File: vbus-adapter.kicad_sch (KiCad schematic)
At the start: 54 parts, among them J1 VBUS, J2 CAN, J3 Sens 2, J4 Sens 1, J5 Power, J6 Backup GPIO, J7 Program, Q1 SS8050, Q2 SS8050, T800 AO3400A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

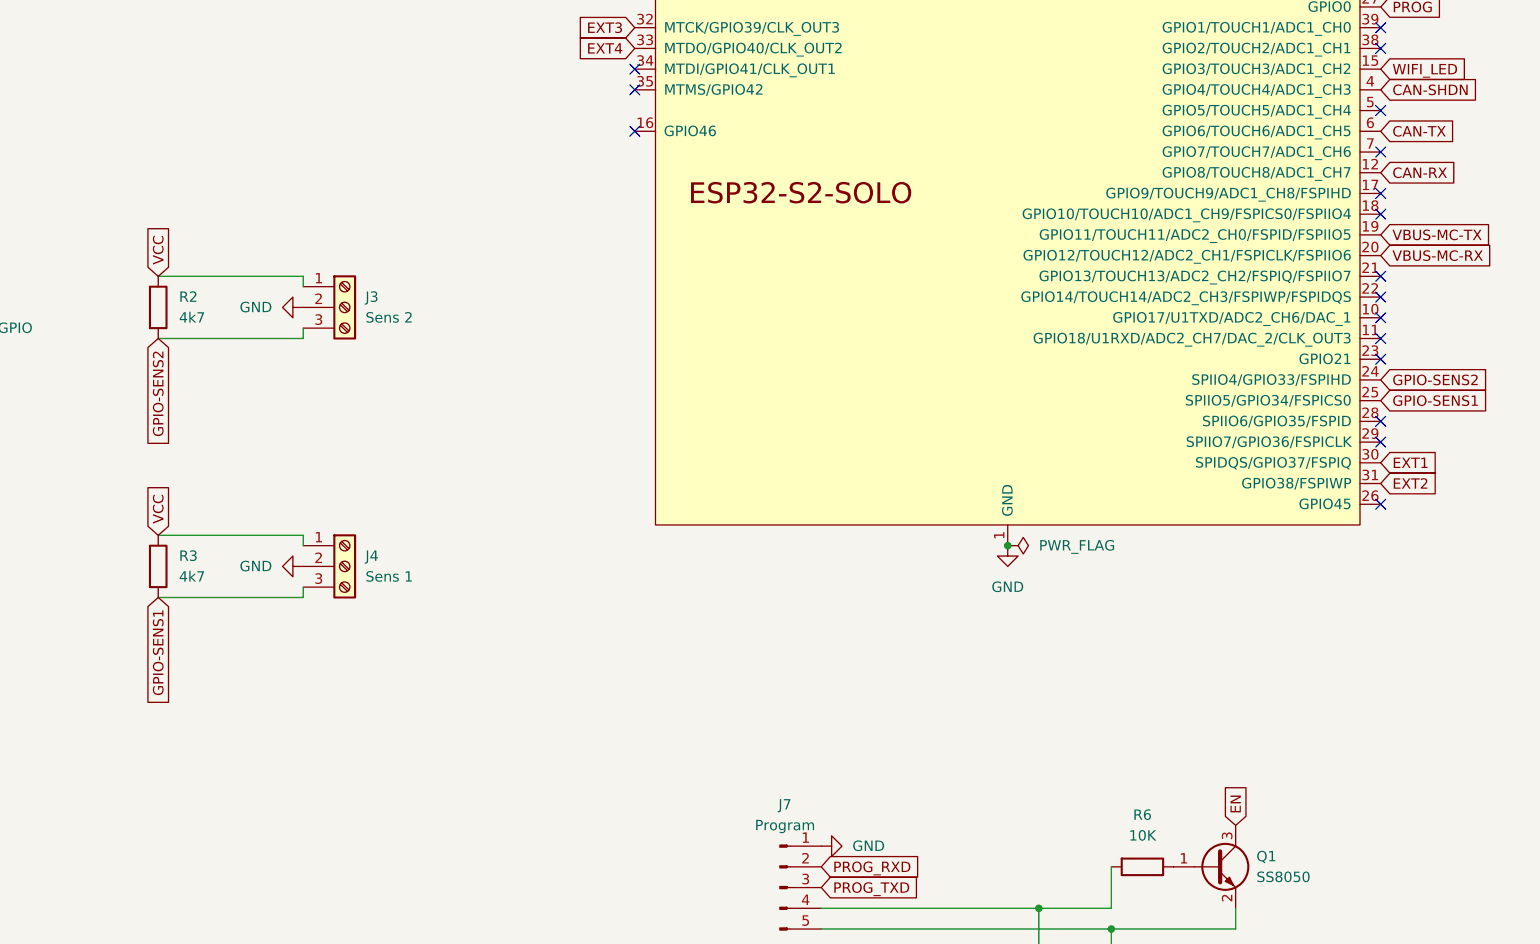
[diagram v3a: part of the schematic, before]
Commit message: Version 5
- Reposition connectors for Programming
- Add +5V to Sensor Connector
- Make VCC on SENS connector from GPIO
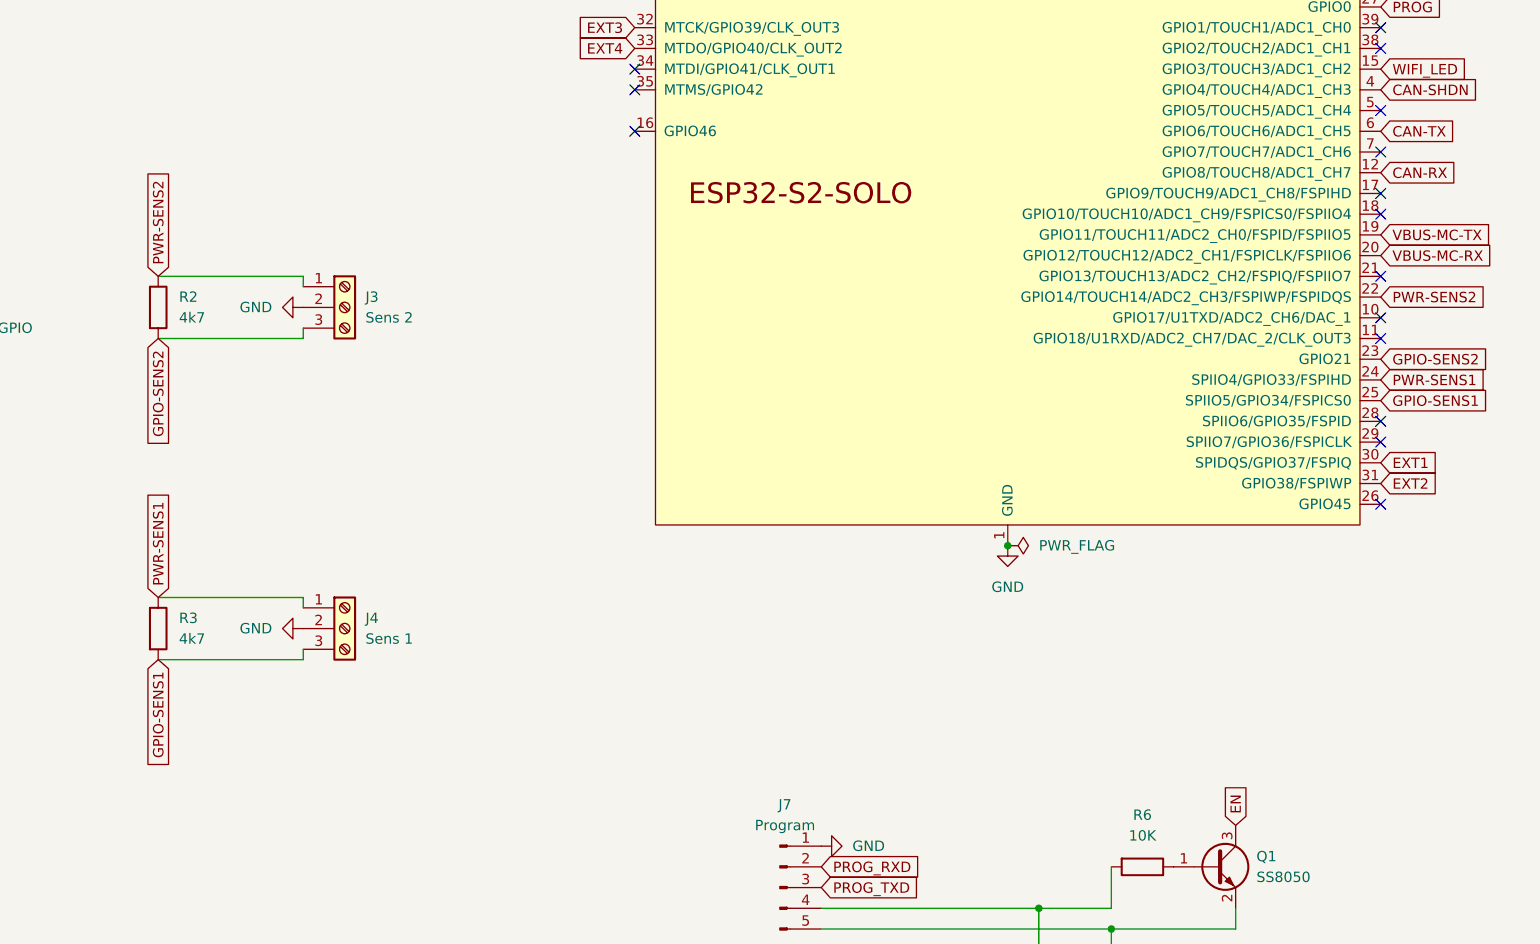
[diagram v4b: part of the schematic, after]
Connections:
- net GPIO-SENS2: now also U2.23 (GPIO21); no longer U2.24 (SPIIO4/GPIO33/FSPIHD)
- net VCC: no longer J3.1 (Pin_1), J4.1 (Pin_1), R2.1, R3.1
- net PWR-SENS2: now reaches U2.22 (GPIO14/TOUCH14/ADC2_CH3/FSPIWP/FSPIDQS)
- net PWR-SENS2: now also J3.1 (Pin_1), R2.1
- new net PWR-SENS1: J4.1 (Pin_1), R3.1, U2.24 (SPIIO4/GPIO33/FSPIHD)
- no-connect marks 22 -> 20
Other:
- moved on the sheet: J4, R3
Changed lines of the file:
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@@
 		(title "vbus-adapter")
 		(date "2026-04-29")
-		(rev "v4")
+		(rev "v5")
 	)
 	(junction
@@
 	)
 	(no_connect
-		(at 370.84 111.76)
-	)
-	(no_connect
 		(at 370.84 91.44)
 	)
@@
 	)
 	(no_connect
-		(at 370.84 104.14)
-	)
-	(no_connect
 		(at 370.84 81.28)
 	)
@@
 	(wire
 		(pts
-			(xy 238.76 140.97) (xy 238.76 139.7)
+			(xy 238.76 148.59) (xy 238.76 147.32)
 		)
 		(stroke
@@
 	(wire
 		(pts
-			(xy 238.76 133.35) (xy 238.76 134.62)
+			(xy 238.76 140.97) (xy 238.76 142.24)
 		)
 		(stroke
@@
 	(wire
 		(pts
-			(xy 220.98 133.35) (xy 238.76 133.35)
+			(xy 220.98 140.97) (xy 238.76 140.97)
 		)
 		(stroke
@@
 	(wire
 		(pts
-			(xy 220.98 140.97) (xy 238.76 140.97)
+			(xy 220.98 148.59) (xy 238.76 148.59)
 		)
 		(stroke
@@
 		)
 	)
+	(global_label "PWR-SENS2"
+		(shape input)
+		(at 220.98 101.6 90)
+		(fields_autoplaced yes)
+		(effects
+			(font
+				(size 1.27 1.27)
+			)
+			(justify left)
+		)
+		(property "Intersheetrefs" "${INTERSHEET_REFS}"
+			(at 220.98 86.943 90)
+			(effects
+				(font
+					(size 1.27 1.27)
+				)
+				(justify left)
+				(hide yes)
+			)
+		)
+	)
 	(global_label "VBUS-MC-TX"
 		(shape input)
@@
 		)
 	)
+	(global_label "PWR-SENS2"
+		(shape input)
+		(at 370.84 104.14 0)
+		(fields_autoplaced yes)
+		(effects
+			(font
+				(size 1.27 1.27)
+			)
+			(justify left)
+		)
+		(property "Intersheetrefs" "${INTERSHEET_REFS}"
+			(at 385.497 104.14 0)
+			(effects
+				(font
+					(size 1.27 1.27)
+				)
+				(justify left)
+				(hide yes)
+			)
+		)
+	)
 	(global_label "EXT1"
 		(shape input)
@@
 		)
 	)
-	(global_label "CAN-SHDN"
+	(global_label "GPIO-SENS2"
 		(shape input)
-		(at 370.84 78.74 0)
+		(at 370.84 111.76 0)
 		(fields_autoplaced yes)
 		(effects
@@
 		)
 		(property "Intersheetrefs" "${INTERSHEET_REFS}"
-			(at 384.2272 78.74 0)
+			(at 385.9809 111.76 0)
 			(effects
 				(font
@@
 		)
 	)
-	(global_label "EN"
+	(global_label "CAN-SHDN"
 		(shape input)
-		(at 279.4 53.34 180)
+		(at 370.84 78.74 0)
 		(fields_autoplaced yes)
 		(effects
@@
 				(size 1.27 1.27)
 			)
-			(justify right)
+			(justify left)
 		)
 		(property "Intersheetrefs" "${INTERSHEET_REFS}"
-			(at 273.9353 53.34 0)
+			(at 384.2272 78.74 0)
 			(effects
 				(font
 					(size 1.27 1.27)
 				)
-				(justify right)
+				(justify left)
 				(hide yes)
 			)
 		)
 	)
-	(global_label "VCC"
+	(global_label "EN"
 		(shape input)
-		(at 220.98 101.6 90)
+		(at 279.4 53.34 180)
 		(fields_autoplaced yes)
 		(effects
@@
 				(size 1.27 1.27)
 			)
-			(justify left)
+			(justify right)
 		)
 		(property "Intersheetrefs" "${INTERSHEET_REFS}"
-			(at 220.98 94.9862 90)
+			(at 273.9353 53.34 0)
 			(effects
 				(font
 					(size 1.27 1.27)
 				)
-				(justify left)
+				(justify right)
 				(hide yes)
 			)
@@
 	(global_label "GPIO-SENS1"
 		(shape input)
-		(at 220.98 140.97 270)
+		(at 220.98 148.59 270)
 		(fields_autoplaced yes)
 		(effects
@@
 		)
 		(property "Intersheetrefs" "${INTERSHEET_REFS}"
-			(at 220.98 156.1109 90)
+			(at 220.98 163.7309 90)
 			(effects
 				(font
@@
 		)
 	)
-	(global_label "VBUS-HI"
-		(shape bidirectional)
-		(at 44.45 46.99 180)
+	(global_label "PWR-SENS1"
+		(shape input)
+		(at 220.98 140.97 90)
 		(fields_autoplaced yes)
 		(effects
@@
 				(size 1.27 1.27)
 			)
-			(justify right)
+			(justify left)
 		)
 		(property "Intersheetrefs" "${INTERSHEET_REFS}"
-			(at 31.9472 46.99 0)
+			(at 220.98 126.313 90)
 			(effects
 				(font
 					(size 1.27 1.27)
 				)
-				(justify right)
+				(justify left)
 				(hide yes)
 			)
 		)
 	)
-	(global_label "GPIO-SENS2"
-		(shape input)
-		(at 370.84 114.3 0)
+	(global_label "VBUS-HI"
+		(shape bidirectional)
+		(at 44.45 46.99 180)
 		(fields_autoplaced yes)
 		(effects
@@
 				(size 1.27 1.27)
 			)
-			(justify left)
+			(justify right)
 		)
 		(property "Intersheetrefs" "${INTERSHEET_REFS}"
-			(at 385.9809 114.3 0)
+			(at 31.9472 46.99 0)
 			(effects
 				(font
 					(size 1.27 1.27)
 				)
-				(justify left)
+				(justify right)
 				(hide yes)
 			)
 		)
 	)
-	(global_label "CAN-RX"
+	(global_label "PWR-SENS1"
 		(shape input)
-		(at 127 167.64 0)
+		(at 370.84 114.3 0)
 		(fields_autoplaced yes)
 		(effects
@@
 		)
 		(property "Intersheetrefs" "${INTERSHEET_REFS}"
-			(at 137.7262 167.64 0)
+			(at 385.497 114.3 0)
 			(effects
 				(font
@@
 		)
 	)
-	(global_label "VCC"
+	(global_label "CAN-RX"
 		(shape input)
-		(at 220.98 133.35 90)
+		(at 127 167.64 0)
 		(fields_autoplaced yes)
 		(effects
@@
 		)
 		(property "Intersheetrefs" "${INTERSHEET_REFS}"
-			(at 220.98 126.7362 90)
+			(at 137.7262 167.64 0)
 			(effects
 				(font
@@
 	(symbol
 		(lib_id "power:GND")
-		(at 238.76 137.16 270)
+		(at 238.76 144.78 270)
 		(unit 1)
 		(exclude_from_sim no)
@@
 		(fields_autoplaced yes)
 		(property "Reference" "#PWR011"
-			(at 232.41 137.16 0)
+			(at 232.41 144.78 0)
 			(effects
 				(font
@@
 		)
 		(property "Value" "GND"
-			(at 234.95 137.1599 90)
+			(at 234.95 144.7799 90)
 			(effects
 				(font
@@
 		)
 		(property "Footprint" ""
-			(at 238.76 137.16 0)
+			(at 238.76 144.78 0)
 			(effects
 				(font
@@
 		)
 		(property "Datasheet" ""
-			(at 238.76 137.16 0)
+			(at 238.76 144.78 0)
 			(effects
 				(font
@@
 		)
 		(property "Description" "Power symbol creates a global label with name \"GND\" , ground"
-			(at 238.76 137.16 0)
+			(at 238.76 144.78 0)
 			(effects
 				(font
@@
 	(symbol
 		(lib_id "Connector:Screw_Terminal_01x03")
-		(at 243.84 137.16 0)
+		(at 243.84 144.78 0)
 		(unit 1)
 		(exclude_from_sim no)
@@
 		(fields_autoplaced yes)
 		(property "Reference" "J4"
-			(at 246.38 135.8899 0)
+			(at 246.38 143.5099 0)
 			(effects
 				(font
@@
 		)
 		(property "Value" "Sens 1"
-			(at 246.38 138.4299 0)
+			(at 246.38 146.0499 0)
 			(effects
 				(font
@@
 		)
 		(property "Footprint" "TerminalBlock_Phoenix:TerminalBlock_Phoenix_MPT-0,5-3-2.54_1x03_P2.54mm_Horizontal"
-			(at 243.84 137.16 0)
+			(at 243.84 144.78 0)
 			(effects
 				(font
@@
 		)
 		(property "Datasheet" "~"
-			(at 243.84 137.16 0)
+			(at 243.84 144.78 0)
 			(effects
 				(font
@@
 		)
 		(property "Description" "Generic screw terminal, single row, 01x03, script generated (kicad-library-utils/schlib/autogen/connector/)"
-			(at 243.84 137.16 0)
+			(at 243.84 144.78 0)
 			(effects
 				(font
@@
 	(symbol
 		(lib_id "Device:R")
-		(at 220.98 137.16 0)
+		(at 220.98 144.78 0)
 		(unit 1)
 		(exclude_from_sim no)
@@
 		(fields_autoplaced yes)
 		(property "Reference" "R3"
-			(at 223.52 135.8899 0)
+			(at 223.52 143.5099 0)
 			(effects
 				(font
@@
 		)
 		(property "Value" "4k7"
-			(at 223.52 138.4299 0)
+			(at 223.52 146.0499 0)
 			(effects
 				(font
@@
 		)
 		(property "Footprint" "Resistor_SMD:R_0805_2012Metric_Pad1.20x1.40mm_HandSolder"
-			(at 219.202 137.16 90)
+			(at 219.202 144.78 90)
 			(effects
 				(font
@@
 		)
 		(property "Datasheet" "~"
-			(at 220.98 137.16 0)
+			(at 220.98 144.78 0)
 			(effects
 				(font
@@
 		)
 		(property "Description" "Resistor"
-			(at 220.98 137.16 0)
+			(at 220.98 144.78 0)
 			(effects
 				(font
@@
 		)
 		(property "Untitled Field" ""
-			(at 220.98 137.16 0)
+			(at 220.98 144.78 0)
 			(effects
 				(font

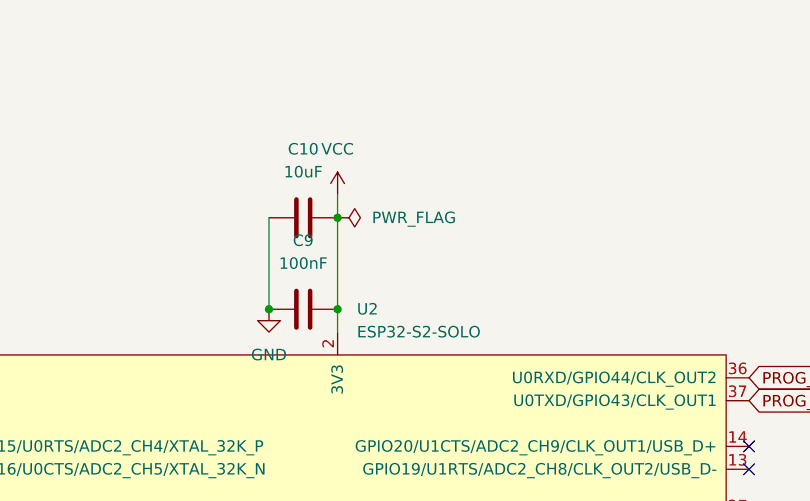
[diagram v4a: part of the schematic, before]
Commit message: Small fixes
- Label placement
- Remove redundant PWR_FLAG
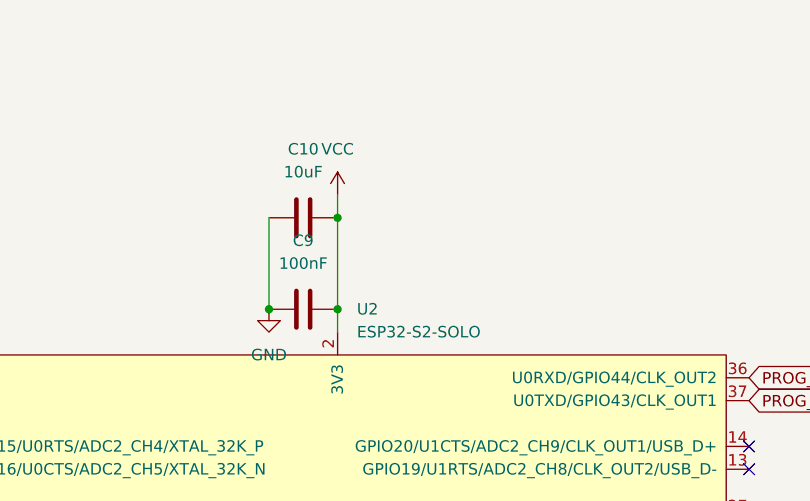
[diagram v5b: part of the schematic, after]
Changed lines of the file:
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@@
-	)
-	(symbol
-		(lib_id "power:PWR_FLAG")
-		(at 325.12 35.56 270)
-		(unit 1)
-		(exclude_from_sim no)
-		(in_bom yes)
-		(on_board yes)
-		(dnp no)
-		(fields_autoplaced yes)
-		(property "Reference" "#FLG05"
-			(at 327.025 35.56 0)
-			(effects
-				(font
-					(size 1.27 1.27)
-				)
-				(hide yes)
-			)
-		)
-		(property "Value" "PWR_FLAG"
-			(at 328.93 35.5599 90)
-			(effects
-				(font
-					(size 1.27 1.27)
-				)
-				(justify left)
-			)
-		)
-		(property "Footprint" ""
-			(at 325.12 35.56 0)
-			(effects
-				(font
-					(size 1.27 1.27)
-				)
-				(hide yes)
-			)
-		)
-		(property "Datasheet" "~"
-			(at 325.12 35.56 0)
-			(effects
-				(font
-					(size 1.27 1.27)
-				)
-				(hide yes)
-			)
-		)
-		(property "Description" "Special symbol for telling ERC where power comes from"
-			(at 325.12 35.56 0)
-			(effects
-				(font
-					(size 1.27 1.27)
-				)
-				(hide yes)
-			)
-		)
-		(pin "1"
-		)
-		(instances
-			(project ""
-				(path "/c5b76d16-c954-491e-a7b2-87b879d4d4be"
-					(reference "#FLG05")
-					(unit 1)
-				)
-			)
-		)
 	)
 	(symbol
